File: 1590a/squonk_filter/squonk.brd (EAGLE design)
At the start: 49.2 x 49.5 mm, 28 parts, among them J1 DC_MONO, Q1 NPN, Q2 NPN

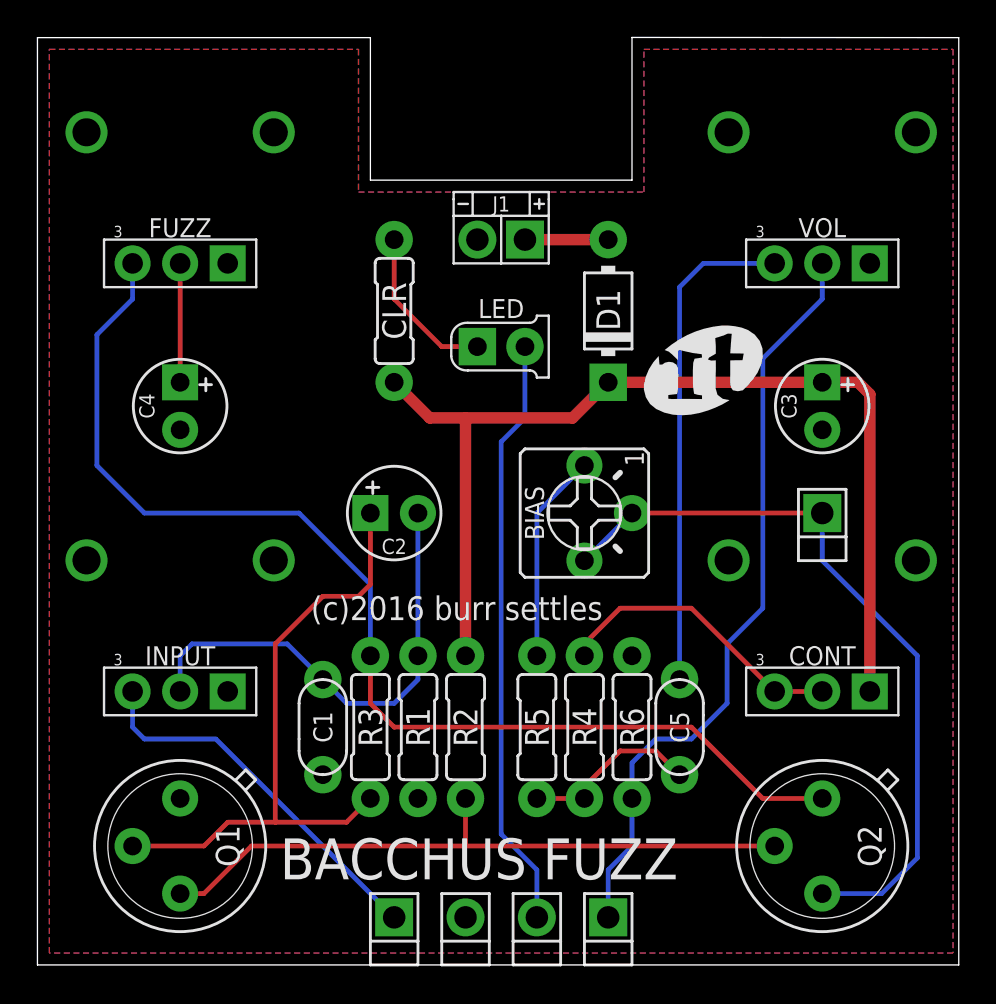
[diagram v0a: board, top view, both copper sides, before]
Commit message: added SQUONK (envelope filter)
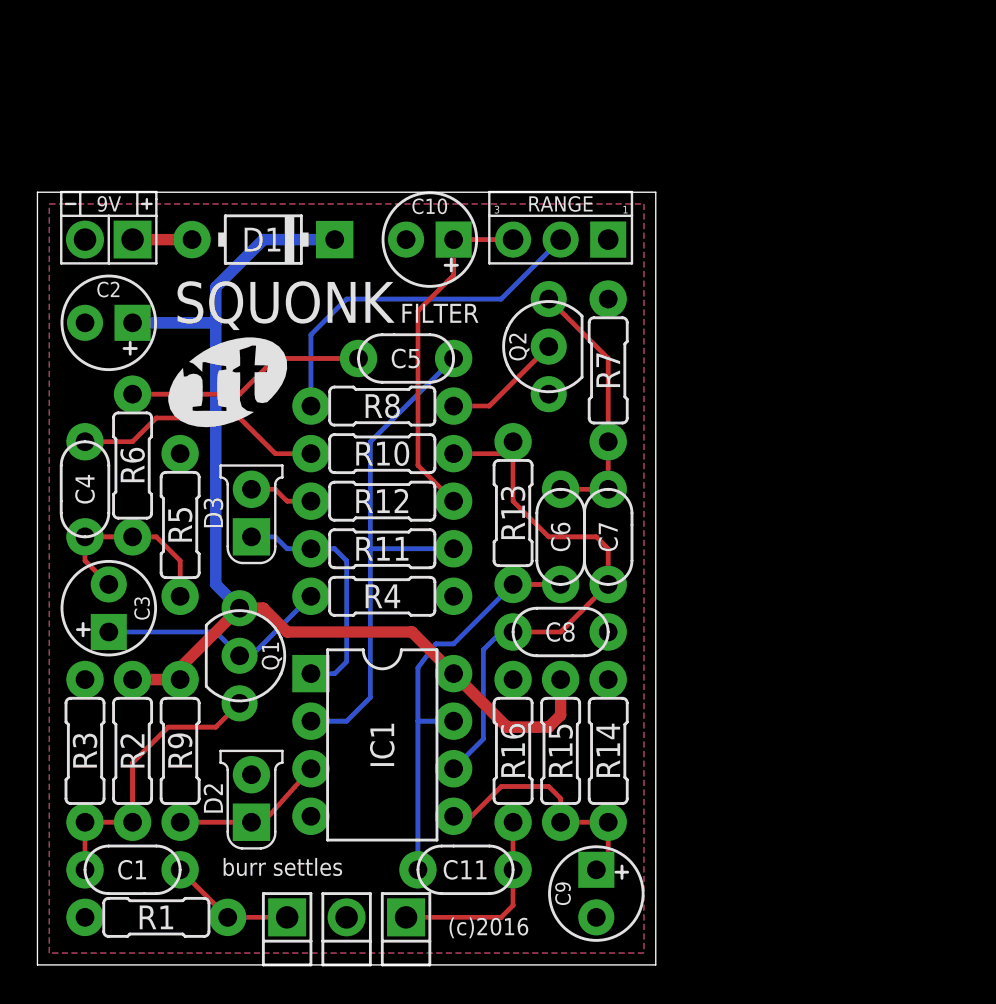
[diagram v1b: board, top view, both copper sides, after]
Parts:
- removed BIAS: 10k, potentiometers:2262_TRIM
- removed CLR: 4k7, resistors:R0207/3
- removed CONT, FUZZ: 1kB, potentiometers:9MM_W/MOUNTS
- removed INPUT: 50kB, potentiometers:9MM_W/MOUNTS
- removed J1: DC_MONO, jacks:DC
- removed L: PADRND, supply pins:ROUND
- removed LED: LEDB, diodes:3MM_B
- removed TP: PADSQR, supply pins:SQUARE
- removed U$4: (no value), logos:RT0250
- removed VOL: 500kA, potentiometers:9MM_W/MOUNTS
- added 9V: DC_MONO, jacks:DC
- added C10: 22u, capacitors-elec:050_020_1
- added C11: 47n, capacitors-film:050X030_025_2
- added C6, C7: 4n7, capacitors-film:050X030_025_2
- added C8: 1n, capacitors-film:050X030_025_2
- added C9: 10u, capacitors-elec:050_020_1
- added D2, D3: LEDB, diodes:3MM_B
- added IC1: TL072, integrated circuits:DIL08
- added R10, R13, R16: 470k, resistors:R0207/3
- added R11: 3M3, resistors:R0207/3
- added R12: 100R, resistors:R0207/3
- added R14, R15, R7: 47k, resistors:R0207/3
- added R8: 22k, resistors:R0207/3
- added R9: 10k, resistors:R0207/3
- added RANGE: 25k, potentiometers:PADS_SMALL
- added U$1: (no value), logos:RT0250
- C1: value 100p -> 47n
- C2: value 2u2 -> 47u
- C3: value 100u -> 10u
- C4: value 22u -> 10n; device capacitors-elec:050_020_1 -> capacitors-film:050X030_025_2
- C5: value 100n -> 47n
- D1: value 2N5817 -> 1N5817
- Q1: value NPN -> MPF102; device transistors:TO5 -> transistors:TO92-
- Q2: value NPN -> 2N4123; device transistors:TO5 -> transistors:TO92-
- R2: value 33k -> 1M
- R3: value 100k -> 1M
- R4: value 220R -> 10k
- R5: value 1k -> 47k
- R6: value 1M -> 47k
- moved C3 39.6 mm to (3.81, 19.1), turned to 90 degrees
- moved Q2 30.4 mm to (27.3, 33.0), turned to 90 degrees
- moved R6 30.1 mm to (5.08, 26.7), turned to 90 degrees
- moved C5 24.5 mm to (19.7, 32.4), turned to 180 degrees
- moved R5 21.9 mm to (7.62, 23.5)
- moved D1 18.8 mm to (12.1, 38.7), turned to 180 degrees
- moved C2 18.3 mm to (3.81, 34.3), turned to 180 degrees
- moved R2 17.8 mm to (5.08, 11.4)
- moved R1 17.3 mm to (6.35, 2.54), turned to 0 degrees
- moved R3 15.3 mm to (2.54, 11.4), turned to 270 degrees
- moved R4 12.9 mm to (18.4, 19.7), turned to 180 degrees
- moved C1 12.7 mm to (5.08, 5.08), turned to 0 degrees
- moved OUT 10.8 mm to (19.7, 2.54)
- moved Q1 10.6 mm to (10.8, 16.5), turned to 270 degrees
- moved C4 6.75 mm to (2.54, 25.4)
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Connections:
- removed net L: L.1, LED.K
- removed net N$12: C5.2, VOL.P$3
- removed net N$15: C4.+, FUZZ.P$2
- removed net N$4: D1.A, J1.T
- removed net N$5: C3.+, CLR.2, CONT.P$1, D1.C, R2.2
- new net N$11: C10.+, R12.2, RANGE.3
- new net N$13: 9V.T, D1.A
- new net N$16: Q2.2, R8.2
- new net N$17: R8.1, RANGE.2
- new net N$19: C6.2, C7.2, Q2.1, R7.2
- new net N$20: C11.2, C6.1, IC1.7, R13.2
- new net N$23: C4.1, R10.1
- new net N$25: C9.+, IC1.5, R14.2, R15.1
- new net VC: C2.+, D1.C, IC1.8, Q1.3, R15.2, R2.2, R9.1
- net GND: now also 9V.S, C10.-, C2.-, C8.2, C9.-, D2.K, IC1.4, Q2.3, R14.1, R16.1, R3.1, R4.1, R5.1, R7.1, RANGE.1; no longer C1.2, C3.-, C4.-, FUZZ.P$1, J1.S, Q1.1, R6.1, VOL.P$1
- net IN: now also C1.2, R1.2; no longer INPUT.P$3
- net N$1: now also Q1.1, R2.1, R3.2; no longer C2.-, INPUT.P$2, R1.2
- net N$10: now also D3.K, R12.1; no longer BIAS.2, BIAS.3, Q2.3, TP.1
- net N$14: now also C7.1, C8.1, IC1.6, R10.2, R13.1; no longer FUZZ.P$3, Q2.1, R3.2
- net N$2: now also C3.+, R4.2; no longer C2.+, R3.1
- net N$3: now also C3.-, C4.2, R5.2, R6.1; no longer Q1.3, Q2.2, R2.1
- net N$6: now also C5.2, R6.2; no longer CONT.P$2, CONT.P$3, R4.1
- net N$7: now also D2.A, IC1.3, R9.2; no longer CLR.1, LED.A
- net N$8: now also IC1.2, R11.1; no longer R4.2, R5.2
- net N$9: now also D3.A, IC1.1, R11.2; no longer BIAS.1, R5.1
- net OUT: now also C11.1, R16.2; no longer R6.2, VOL.P$2
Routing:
- net VC: track 0.00 -> 59.1 mm
- net N$5: track 55.8 -> 0.00 mm
- net N$10: track 40.1 -> 3.44 mm
- net L: track 31.8 -> 0.00 mm
- net N$14: track 61.4 -> 29.8 mm
- net OUT: track 40.8 -> 10.4 mm
- net N$12: track 26.6 -> 0.00 mm
- net N$3: track 35.3 -> 10.6 mm
- net N$20: track 0.00 -> 22.3 mm
- net N$2: track 33.5 -> 12.6 mm
- net N$17: track 0.00 -> 19.2 mm
- net N$11: track 0.00 -> 18.7 mm
- net N$8: track 9.57 -> 28.1 mm
- net N$19: track 0.00 -> 14.0 mm
- net N$23: track 0.00 -> 13.4 mm
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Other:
- board size 49.2 x 49.5 mm -> 33 x 41.3 mm
- board text added: "(c)2016"
- board text added: "FILTER"
- board text added: "SQUONK"
- board text added: "burr settles"
- board text removed: "(c)2016 burr settles"
- board text removed: "BACCHUS FUZZ"

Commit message: updated library + logos
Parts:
- U$1: device logos:RT0250 -> logos:BF0150
- moved U$1 1.42 mm to (10.8, 29.8)
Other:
- board text added: "http://bffx.us"
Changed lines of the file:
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@@
 <wire x1="33.02" y1="41.265" x2="0" y2="41.265" width="0" layer="20"/>
 <wire x1="0" y1="41.265" x2="0" y2="0" width="0" layer="20"/>
-<text x="7.3025" y="34.29" size="2.1844" layer="21">SQUONK</text>
+<text x="6.985" y="34.29" size="2.1844" layer="21">SQUONK</text>
 <text x="21.9075" y="1.5875" size="0.9144" layer="21">(c)2016</text>
 <text x="19.3675" y="34.29" size="1.016" layer="21">FILTER</text>
-<text x="9.8425" y="4.7625" size="0.9144" layer="21">burr settles</text>
+<text x="9.2075" y="4.7625" size="0.9144" layer="21">http://bffx.us</text>
+<text x="6.985" y="32.7025" size="0.9144" layer="21">burr settles</text>
 </plain>
 <attributes>
@@
 <element name="D2" library="diodes" package="3MM_B" value="LEDB" x="11.43" y="8.89" rot="R90"/>
 <element name="R1" library="resistors" package="R0207/3" value="1M" x="6.35" y="2.54"/>
-<element name="U$1" library="logos" package="RT0250" value="" x="10.16" y="31.115"/>
+<element name="U$1" library="logos" package="BF0150" value="" x="10.795" y="29.845"/>
 </elements>
 <signals>
